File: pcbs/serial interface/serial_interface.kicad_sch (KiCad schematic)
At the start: 24 parts, among them J1 AFBR-1624Z, J2 AFBR-2624Z, U1 MM232R, U2 UMFT234XF, U3 74LVC1G14, U4 74LVC1G14

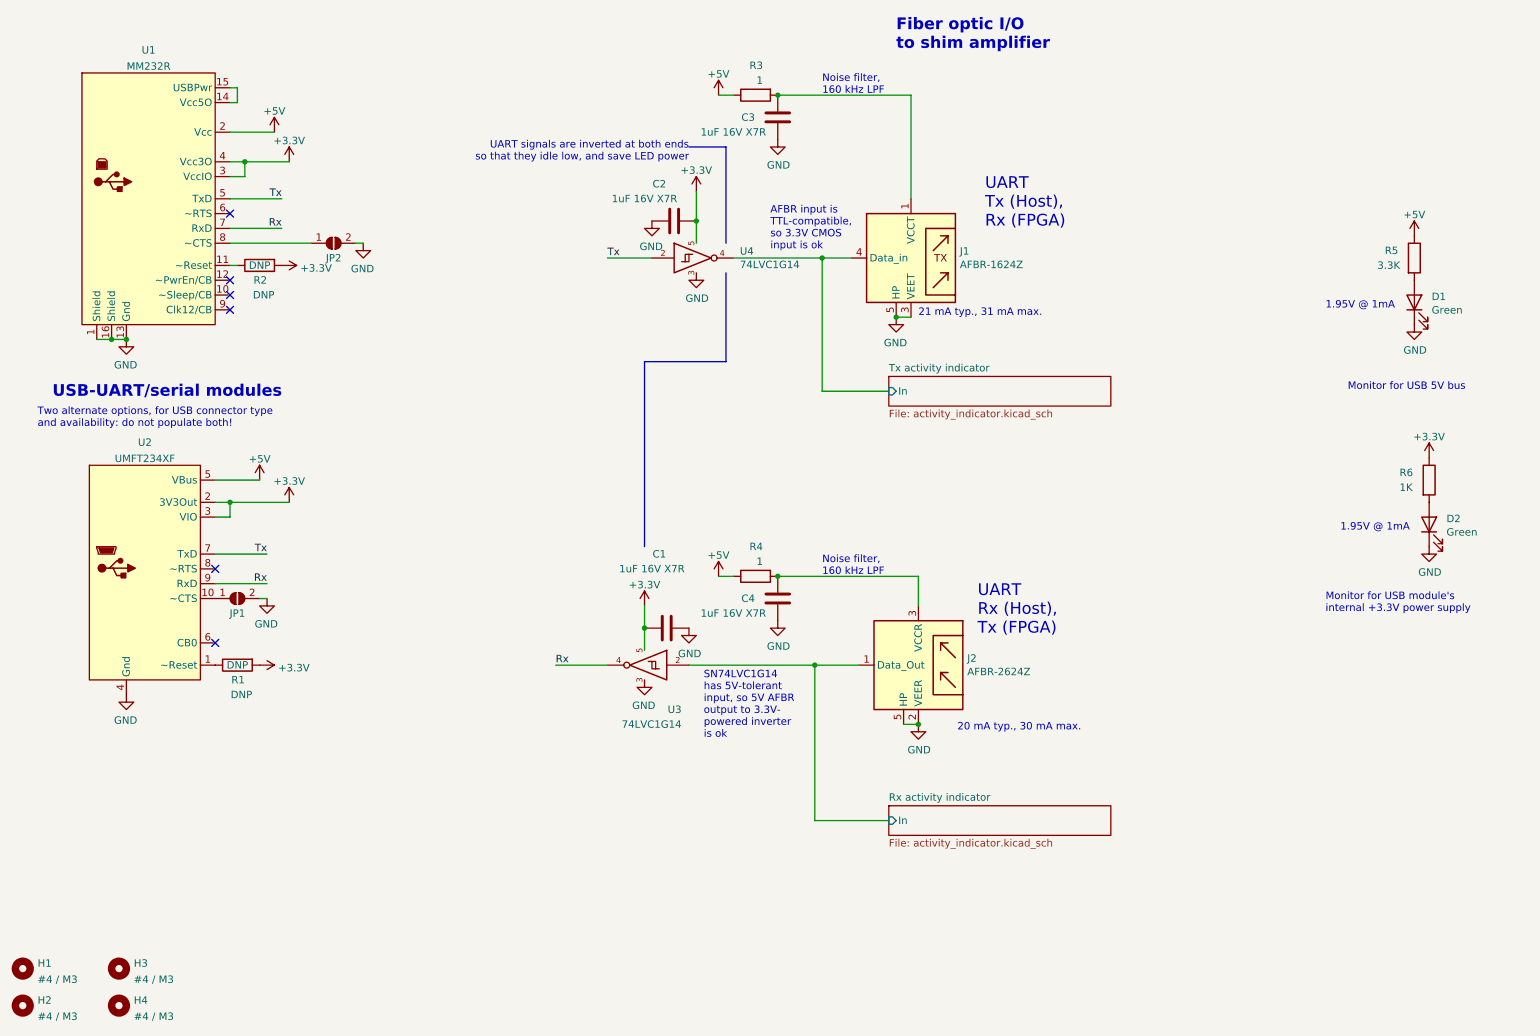
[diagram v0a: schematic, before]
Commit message: Serial interface speed improvement
Upgraded serial interface to KiCAD 7.0
Replaced USB-serial modules with higher-speed (12 Mbps) one (#7)
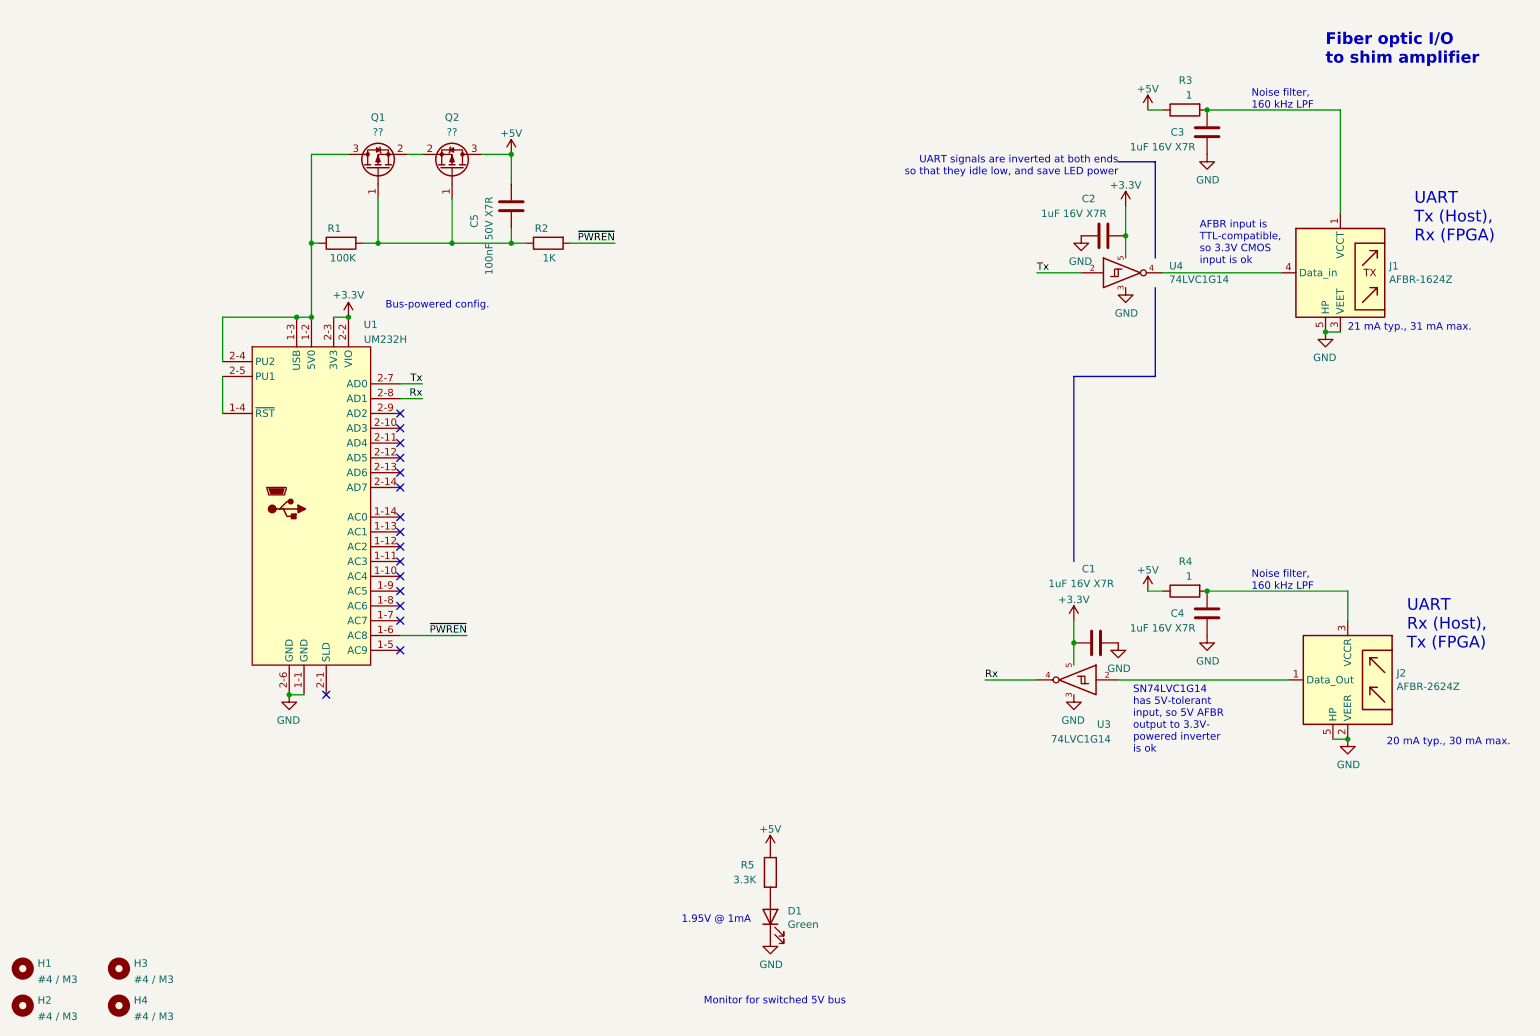
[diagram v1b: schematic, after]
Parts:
- removed D2: Green, Martinos_std:LED_0805_2012Metric, symbol Device:LED
- removed JP1, JP2: SolderJumper_2_Open, Jumper:SolderJumper-2_P1.3mm_Open_TrianglePad1.0x1.5mm, symbol Jumper:SolderJumper_2_Open
- removed R6: 1K, Resistor_SMD:R_0805_2012Metric, symbol Device:R
- removed U1: MM232R, Martinos:FTDI_MM232R, symbol Martinos:MM232R
- removed U2: UMFT234XF, Martinos:FTDI_UMFT234XF, symbol Martinos:UMFT234XF
- added C5: 100nF 50V X7R, Capacitor_SMD:C_0603_1608Metric, symbol Device:C
- added Q1, Q2: ??, Package_TO_SOT_SMD:SOT-23, symbol Transistor_FET:DMG2301L
- added U1: UM232H, Don:FTDI_UM232H, symbol Don:UM232H
- R1: value DNP -> 100K; DNP DNP -> (none)
- R2: value DNP -> 1K; DNP DNP -> (none)
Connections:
- net +3V3: now also U1.2-2 (VIO), U1.2-3 (3V3); no longer R1.2, R2.2
- net +5V: now also C5.2, Q2.3 (D)
- net GND: now also U1.1-1 (GND), U1.2-6 (GND)
- net Rx: now also U1.2-8 (AD1)
- net Tx: now also U1.2-7 (AD0)
- net at R2.1: now also R1.2, C5.1, Q1.1 (G), Q2.1 (G)
- net at R1.1: now also Q1.3 (D), U1.1-2 (5V0), U1.1-3 (USB), U1.2-4 (PU2)
- net Rx activity indicator/In: no longer names the net of J2.1 (Data_Out), U3.2
- net Tx activity indicator/In: no longer names the net of J1.4 (Data_in), U4.4
- new net: Q1.2 (S), Q2.2 (S)
- new net: U1.1-4 (~{RST}), U1.2-5 (PU1)
- new net ~{PWREN}: R2.2, U1.1-6 (AC8)
- no-connect marks 6 -> 16
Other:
- removed sheet Rx activity indicator
- removed sheet Tx activity indicator
- note added: "Bus-powered config."
- note added: "Monitor for switched 5V bus"
- note removed: "Monitor for USB 5V bus"
- note removed: "Monitor for USB module's internal +3.3V power supply"
- note removed: "Two alternate options, for USB connector type and availability: do not populate both!"
- note removed: "USB-UART/serial modules"
- moved on the sheet: C1, C2, C3, C4, D1, J1, J2, R3, R4, R5, U3, U4

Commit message: Misc. mfg
Marked top-side testpoints on amp control board as DNP
Updated serial interface board's BOM-placement-help file
Exported stiffener file for amp control board
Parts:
- Q1, Q2: value ?? -> DMG2305UX or similar
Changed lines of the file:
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@@
       (effects (font (size 1.27 1.27)))
     )
-    (property "Value" "??" (at 82.55 36.83 90)
+    (property "Value" "DMG2305UX or similar" (at 82.55 36.83 90)
       (effects (font (size 1.27 1.27)))
     )
@@
   (symbol (lib_id "Transistor_FET:DMG2301L") (at 95.25 43.18 270) (mirror x) (unit 1)
     (in_bom yes) (on_board yes) (dnp no)
-    (property "Reference" "Q2" (at 95.25 34.29 90)
-      (effects (font (size 1.27 1.27)))
-    )
-    (property "Value" "??" (at 95.25 36.83 90)
-      (effects (font (size 1.27 1.27)))
-    )
+    (property "Reference" "Q2" (at 95.25 29.21 90)
+      (effects (font (size 1.27 1.27)))
+    )
+    (property "Value" "DMG2305UX or similar" (at 95.25 31.75 90)
+      (effects (font (size 1.27 1.27)))
+    )

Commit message: Moved all project-specific symbols & footprints into new "shim" libraries Updated projects to reference the new "shim" library
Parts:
- D1: footprint Martinos_std:LED_0805_2012Metric -> shim:LED_0805_2012Metric
- J1, J2: footprint Martinos:AFBR-xx2xZ -> shim:AFBR-xx2xZ
- U1: footprint Don:FTDI_UM232H -> shim:FTDI_UM232H; symbol Don:UM232H -> shim:UM232H
- U3, U4: footprint Martinos_std:SOT-23-5 -> Package_TO_SOT_SMD:SOT-23-5; symbol Martinos:74LVC1G14 -> shim:74LVC1G14
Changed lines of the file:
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@@
 			)
 		)
-		(property "Footprint" "Martinos:AFBR-xx2xZ"
+		(property "Footprint" "shim:AFBR-xx2xZ"
 			(at 247.65 76.2 0)
 			(effects
@@
 			)
 		)
-		(property "Footprint" "Martinos_std:LED_0805_2012Metric"
+		(property "Footprint" "shim:LED_0805_2012Metric"
 			(at 149.86 171.45 0)
 			(effects
@@
 	)
 	(symbol
-		(lib_id "Martinos:74LVC1G14")
+		(lib_id "shim:74LVC1G14")
 		(at 201.93 130.81 0)
 		(mirror y)
@@
 			)
 		)
-		(property "Footprint" "Martinos_std:SOT-23-5"
+		(property "Footprint" "Package_TO_SOT_SMD:SOT-23-5"
 			(at 201.93 130.81 0)
 			(effects
@@
 			)
 		)
-		(property "Footprint" "Martinos:AFBR-xx2xZ"
+		(property "Footprint" "shim:AFBR-xx2xZ"
 			(at 251.46 143.51 0)
 			(effects
@@
 	)
 	(symbol
-		(lib_id "Don:UM232H")
+		(lib_id "shim:UM232H")
 		(at 71.12 100.33 0)
 		(unit 1)
@@
 			)
 		)
-		(property "Footprint" "Don:FTDI_UM232H"
+		(property "Footprint" "shim:FTDI_UM232H"
 			(at 71.12 91.44 0)
 			(effects
@@
 	)
 	(symbol
-		(lib_id "Martinos:74LVC1G14")
+		(lib_id "shim:74LVC1G14")
 		(at 210.82 60.96 0)
 		(unit 1)
@@
 			)
 		)
-		(property "Footprint" "Martinos_std:SOT-23-5"
+		(property "Footprint" "Package_TO_SOT_SMD:SOT-23-5"
 			(at 210.82 60.96 0)
 			(effects
